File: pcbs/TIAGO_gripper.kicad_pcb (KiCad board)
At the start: 4 copper layers, 62 x 60 mm, 60 parts, among them J1 USB_C_Receptacle_USB2.0, J2 Conn_01x02_Pin, J3 S3B-XH-ALFSN, J4 Conn_02x05_Counter_Clockwise, U1 ESP32-C3-MINI-1, U2 SP3485EN-L/TR, U4 RY8411, U5 SRV05-4, U6 TPS54340DDAR

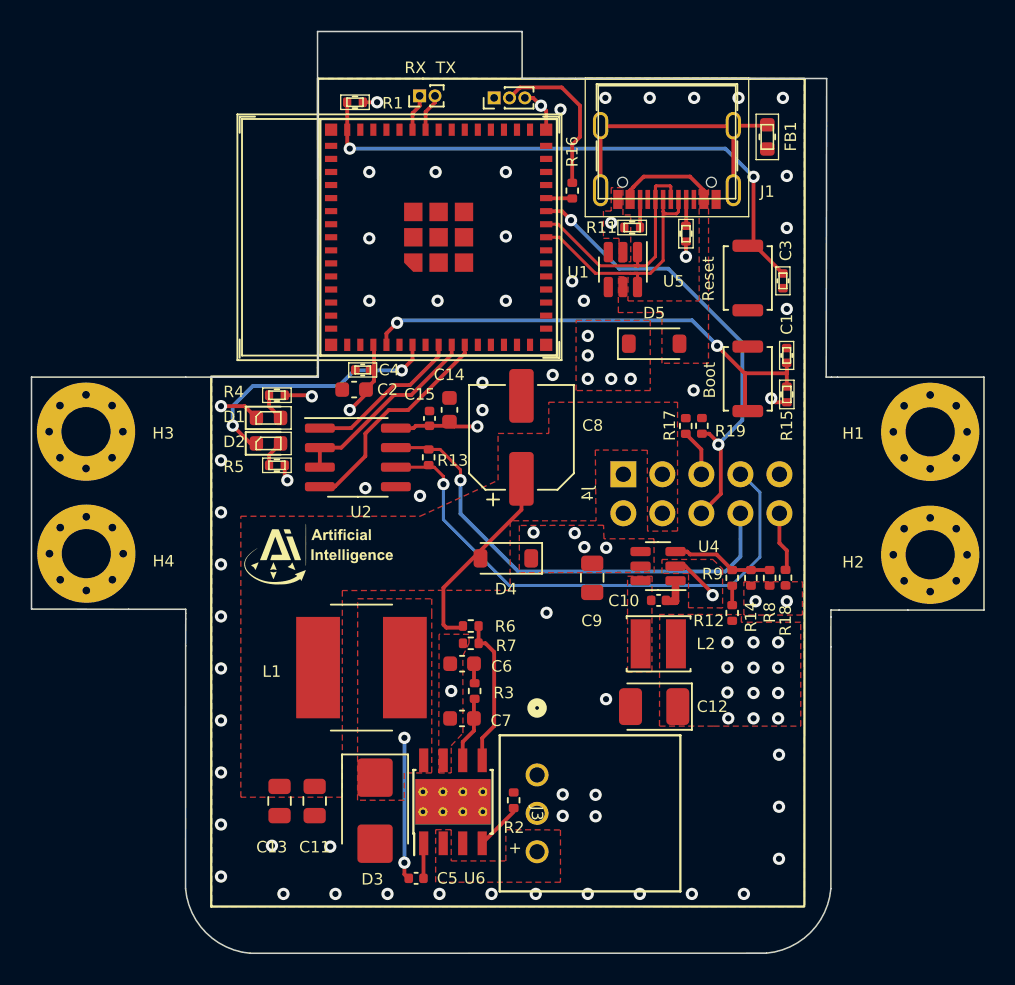
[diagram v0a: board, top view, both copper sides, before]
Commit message: 1.Fix Rs485 communicaton
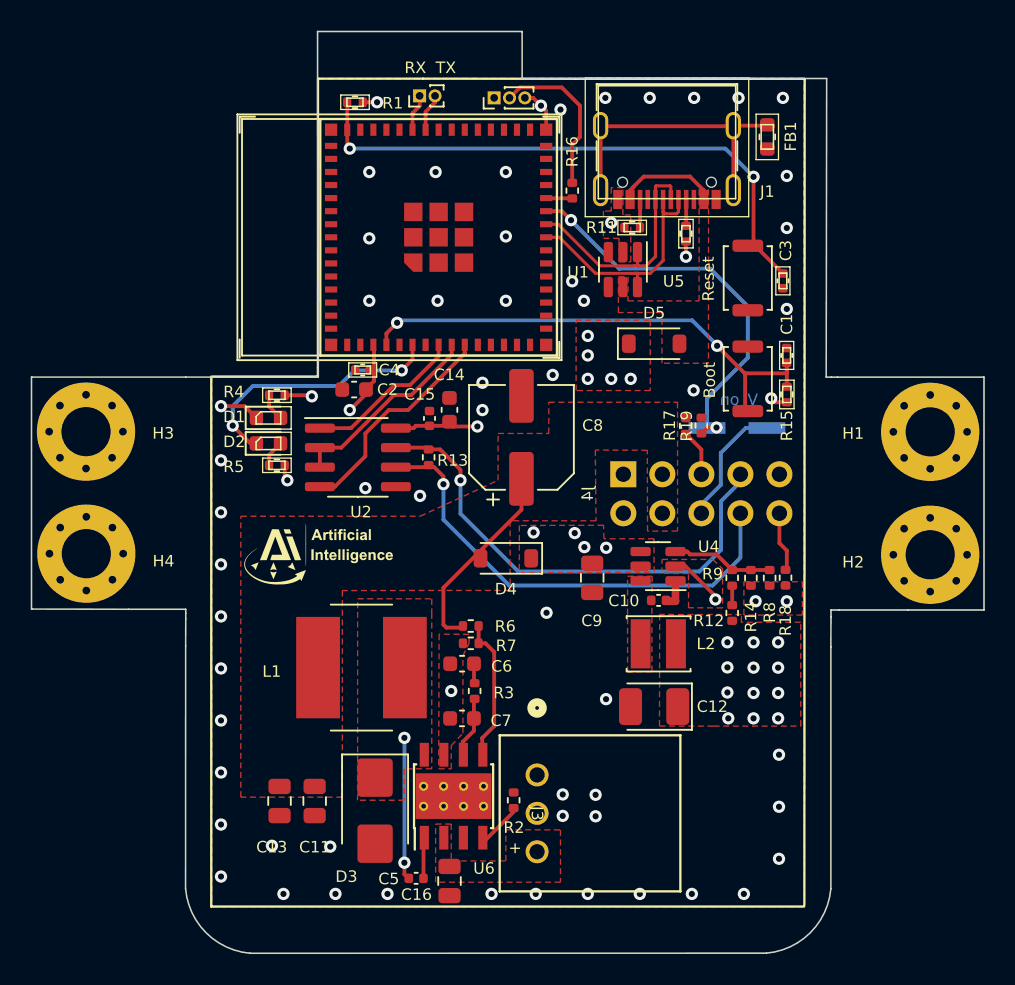
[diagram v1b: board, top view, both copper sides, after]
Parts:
- added C16: 2.2uF, Capacitor_SMD:C_0805_2012Metric, F.Cu at (125.1, 115.2)
- added J5: Conn_01x02_Pin, Connector_PinHeader_1.27mm:PinHeader_2x01_P1.27mm_Vertical_SMD, B.Cu at (143.8, 85.8)
- U6: value TPS54340DDAR -> TPS54340BDDAR
- moved U6 0.36 mm to (125.4, 109.7)
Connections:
- J4 pad 6: V_on -> V_on_p
- J4 pad 7: 485+ -> 485-
- J4 pad 8: 485- -> 485+
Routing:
- net V_on_p: track 0.00 -> 8.13 mm
- net 485+: track 36.3 -> 30.9 mm
- net V_on: track 30.1 -> 25.9 mm
- net 485-: track 30.8 -> 33.4 mm
- net GND: track 9.84 -> 10.2 mm, vias 63 -> 62
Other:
- board text added: "V_on"

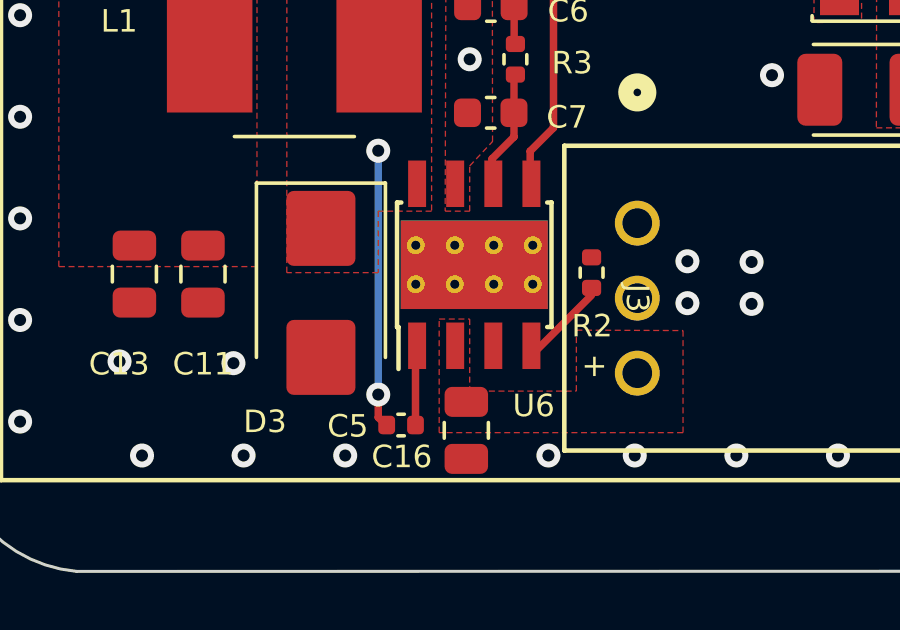
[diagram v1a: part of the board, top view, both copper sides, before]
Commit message: Change DC-DC converter to 60V version
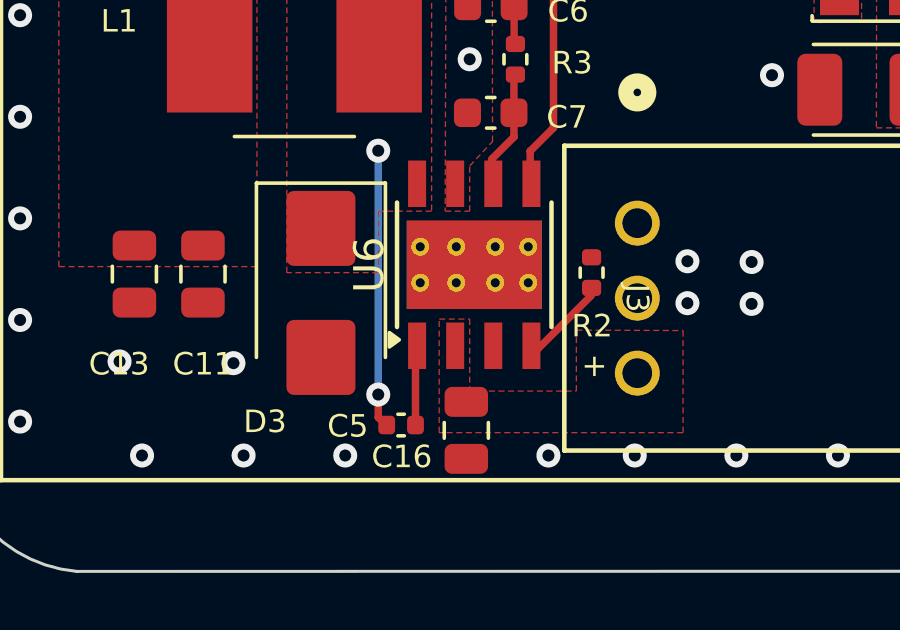
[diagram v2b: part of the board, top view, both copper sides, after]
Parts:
- U6: value TPS54340BDDAR -> TPS54360BDDAR; footprint Package_SO:Texas_HSOP-8-1EP_3.9x4.9mm_P1.27mm_ThermalVias -> Package_SO:TI_SO-PowerPAD-8_ThermalVias
